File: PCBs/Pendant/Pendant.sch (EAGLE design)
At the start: 17 parts

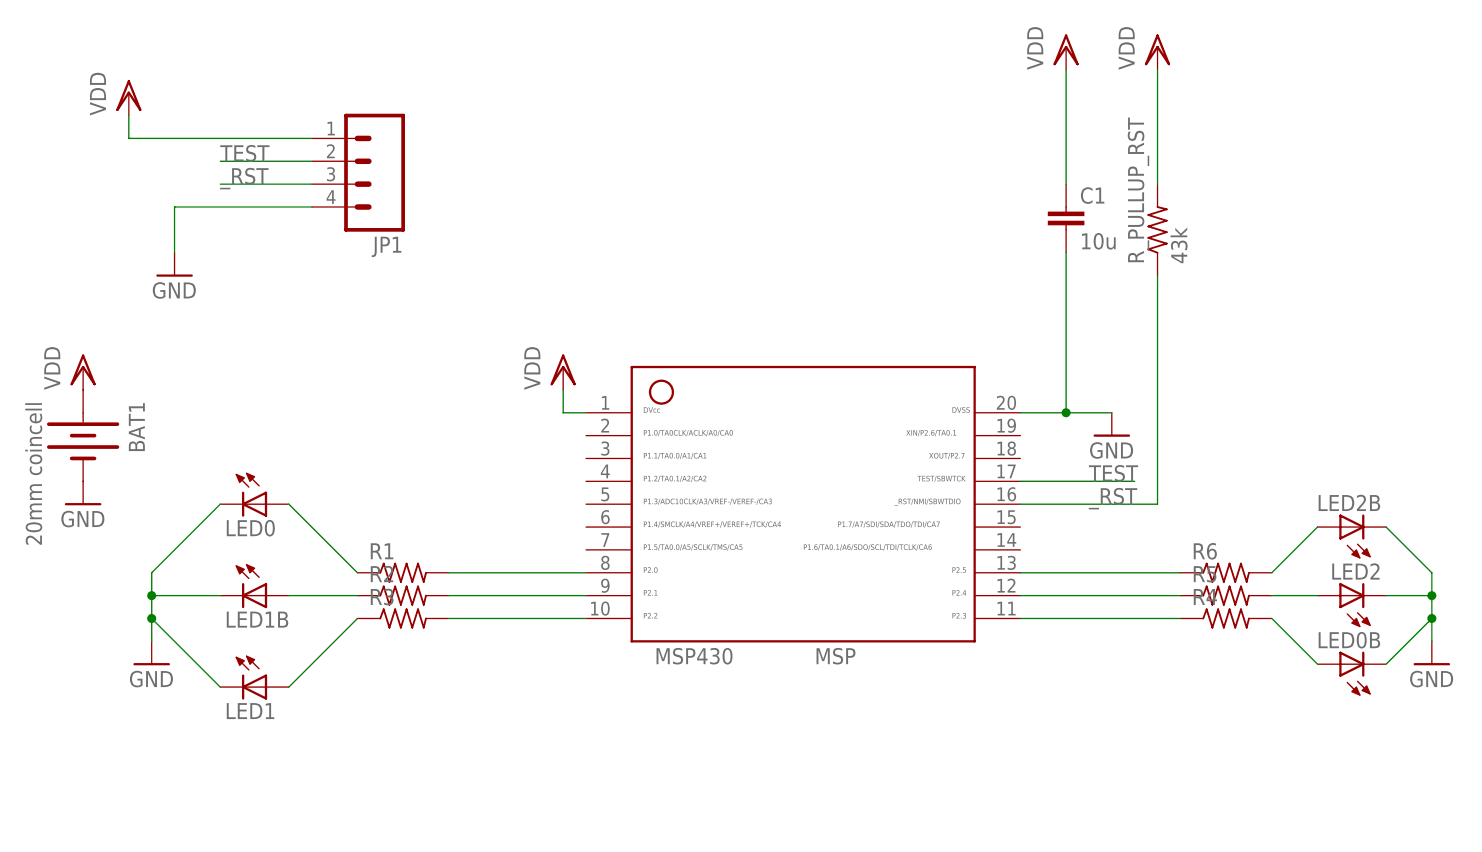
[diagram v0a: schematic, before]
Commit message: Updated pendant to 2017 version
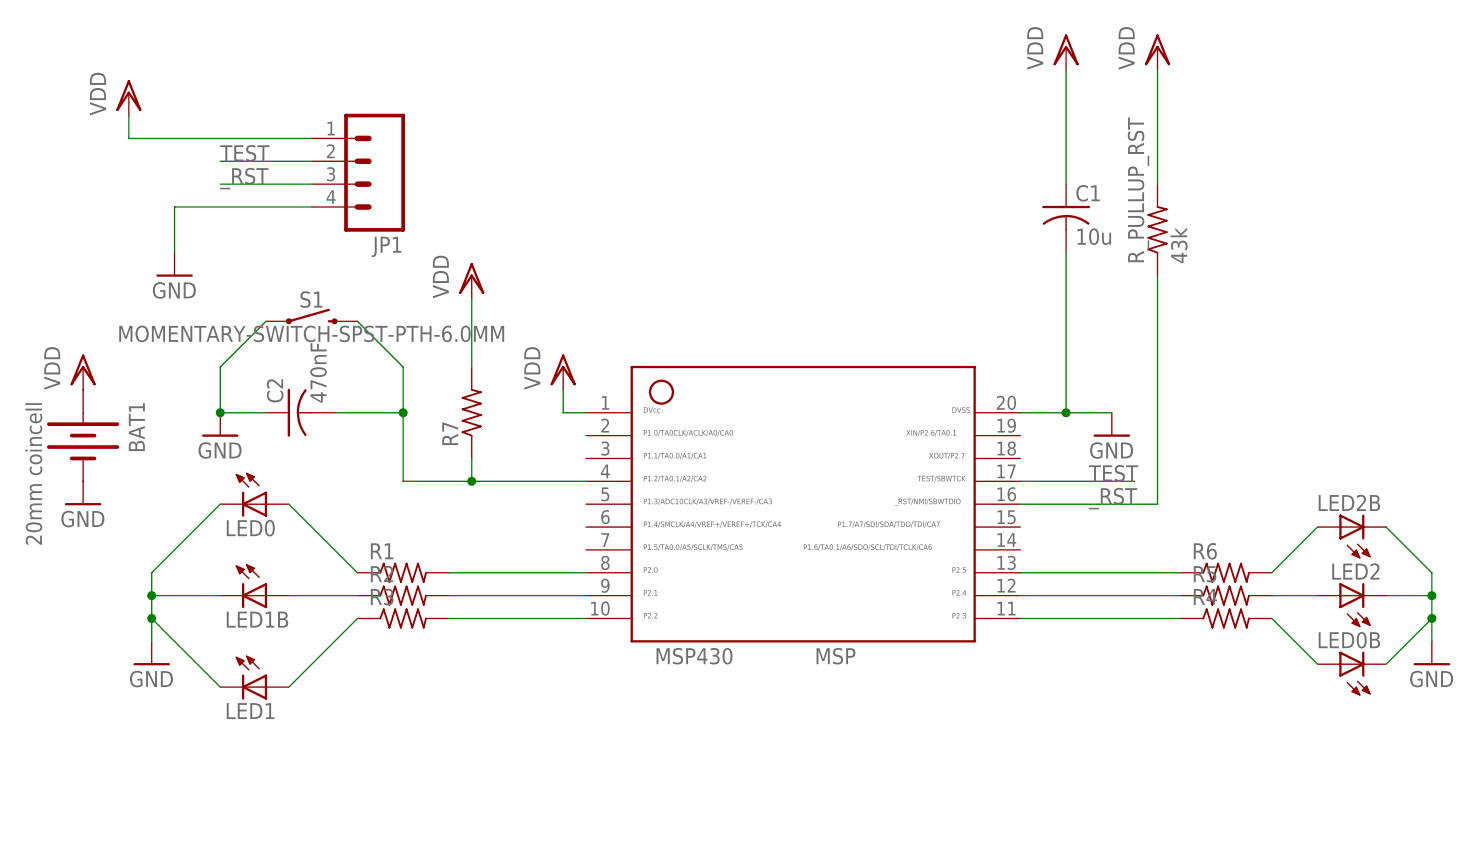
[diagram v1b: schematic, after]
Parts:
- added C2: 470nF, rcl:C-USC1206
- added R7: (no value), rcl:R-US_R1206
- added S1: MOMENTARY-SWITCH-SPST-PTH-6.0MM, SparkFun-Switches:MOMENTARY-SWITCH-SPST-PTH-6.0MM
- C1: device rcl:C-EUC0603 -> rcl:C-USC1206
- R1, R2, R3, R4, R5, R6, R_PULLUP_RST: device BiphasicBoard:R-US_R0603 -> rcl:R-US_R1206
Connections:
- new net N$14: C2.2, MSP430.4, R7.1, S1.2
- net GND: now also C2.1, S1.1
- net VDD: now also R7.2
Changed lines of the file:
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@@
 <?xml version="1.0" encoding="utf-8"?>
 <!DOCTYPE eagle SYSTEM "eagle.dtd">
-<eagle version="7.5.0">
+<eagle version="7.7.0">
 <drawing>
 <settings>
@@
 <layer number="113" name="IDFDebug" color="4" fill="1" visible="no" active="yes"/>
 <layer number="116" name="Patch_BOT" color="9" fill="4" visible="yes" active="yes"/>
+<layer number="118" name="Rect_Pads" color="7" fill="1" visible="no" active="yes"/>
 <layer number="121" name="tTestdril" color="7" fill="1" visible="yes" active="yes"/>
 <layer number="122" name="bTestdril" color="7" fill="1" visible="yes" active="yes"/>
@@
 <layer number="251" name="SMDround" color="12" fill="11" visible="no" active="no"/>
 <layer number="254" name="OrgLBR" color="7" fill="1" visible="yes" active="yes"/>
+<layer number="255" name="routoute" color="7" fill="1" visible="no" active="yes"/>
 </layers>
 <schematic xreflabel="%F%N/%S.%C%R" xrefpart="/%S.%C%R">
@@
 </classes>
 <parts>
-<part name="R_PULLUP_RST" library="BiphasicBoard" deviceset="R-US_" device="R0603" value="43k"/>
+<part name="R_PULLUP_RST" library="rcl" deviceset="R-US_" device="R1206" value="43k"/>
 <part name="MSP430" library="RatDBS" deviceset="MSP430" device="" value="MSP"/>
 <part name="LED2B" library="SparkFun-LED" deviceset="LED" device="1206"/>
-<part name="R6" library="BiphasicBoard" deviceset="R-US_" device="R0603"/>
+<part name="R6" library="rcl" deviceset="R-US_" device="R1206"/>
 <part name="JP1" library="Pendant" deviceset="M04" device="LOCK"/>
 <part name="VDD1" library="supply1" deviceset="VDD" device=""/>
@@
 <part name="VDD11" library="supply1" deviceset="VDD" device=""/>
 <part name="GND11" library="supply1" deviceset="GND" device=""/>
-<part name="C1" library="rcl" deviceset="C-EU" device="C0603" value="10u"/>
-<part name="R1" library="BiphasicBoard" deviceset="R-US_" device="R0603"/>
-<part name="R2" library="BiphasicBoard" deviceset="R-US_" device="R0603"/>
-<part name="R3" library="BiphasicBoard" deviceset="R-US_" device="R0603"/>
-<part name="R5" library="BiphasicBoard" deviceset="R-US_" device="R0603"/>
-<part name="R4" library="BiphasicBoard" deviceset="R-US_" device="R0603"/>
+<part name="C1" library="rcl" deviceset="C-US" device="C1206" value="10u"/>
+<part name="R1" library="rcl" deviceset="R-US_" device="R1206"/>
+<part name="R2" library="rcl" deviceset="R-US_" device="R1206"/>
+<part name="R3" library="rcl" deviceset="R-US_" device="R1206"/>
+<part name="R5" library="rcl" deviceset="R-US_" device="R1206"/>
+<part name="R4" library="rcl" deviceset="R-US_" device="R1206"/>
 <part name="LED2" library="SparkFun-LED" deviceset="LED" device="1206"/>
 <part name="LED0B" library="SparkFun-LED" deviceset="LED" device="1206"/>
@@
 <part name="GND1" library="supply1" deviceset="GND" device=""/>
 <part name="GND2" library="supply1" deviceset="GND" device=""/>
+<part name="S1" library="SparkFun-Switches" deviceset="MOMENTARY-SWITCH-SPST" device="-PTH-6.0MM"/>
+<part name="VDD2" library="supply1" deviceset="VDD" device=""/>
+<part name="R7" library="rcl" deviceset="R-US_" device="R1206"/>
+<part name="GND3" library="supply1" deviceset="GND" device=""/>
+<part name="C2" library="rcl" deviceset="C-US" device="C1206" value="470nF"/>
 </parts>
 <sheets>
@@
 <instance part="GND1" gate="1" x="-71.12" y="-17.78"/>
 <instance part="GND2" gate="1" x="71.12" y="-17.78"/>
+<instance part="S1" gate="G$1" x="-53.34" y="20.32"/>
+<instance part="VDD2" gate="G$1" x="-35.56" y="25.4"/>
+<instance part="R7" gate="G$1" x="-35.56" y="10.16" rot="R90"/>
+<instance part="GND3" gate="1" x="-63.5" y="7.62"/>
+<instance part="C2" gate="G$1" x="-55.88" y="10.16" rot="R90"/>
 </instances>
 <busses>
@@
 <pinref part="BAT1" gate="G$1" pin="+"/>
 <pinref part="VDD11" gate="G$1" pin="VDD"/>
+</segment>
+<segment>
+<pinref part="VDD2" gate="G$1" pin="VDD"/>
+<pinref part="R7" gate="G$1" pin="2"/>
+<wire x1="-35.56" y1="22.86" x2="-35.56" y2="15.24" width="0.1524" layer="91"/>
 </segment>
 </net>
@@
 <pinref part="GND6" gate="1" pin="GND"/>
 </segment>
+<segment>
+<pinref part="S1" gate="G$1" pin="1"/>
+<wire x1="-58.42" y1="20.32" x2="-63.5" y2="15.24" width="0.1524" layer="91"/>
+<wire x1="-63.5" y1="15.24" x2="-63.5" y2="10.16" width="0.1524" layer="91"/>
+<pinref part="GND3" gate="1" pin="GND"/>
+<pinref part="C2" gate="G$1" pin="1"/>
+<wire x1="-58.42" y1="10.16" x2="-63.5" y2="10.16" width="0.1524" layer="91"/>
+<junction x="-63.5" y="10.16"/>
+</segment>
 </net>
 <net name="TEST" class="0">
@@
 </segment>
 </net>
+<net name="N$14" class="0">
+<segment>
+<pinref part="R7" gate="G$1" pin="1"/>
+<wire x1="-35.56" y1="5.08" x2="-35.56" y2="2.54" width="0.1524" layer="91"/>
+<pinref part="MSP430" gate="G$1" pin="4"/>
+<wire x1="-35.56" y1="2.54" x2="-22.86" y2="2.54" width="0.1524" layer="91"/>
+<pinref part="S1" gate="G$1" pin="2"/>
+<wire x1="-48.26" y1="20.32" x2="-43.18" y2="15.24" width="0.1524" layer="91"/>
+<wire x1="-43.18" y1="15.24" x2="-43.18" y2="10.16" width="0.1524" layer="91"/>
+<wire x1="-43.18" y1="10.16" x2="-43.18" y2="2.54" width="0.1524" layer="91"/>
+<wire x1="-43.18" y1="2.54" x2="-35.56" y2="2.54" width="0.1524" layer="91"/>
+<junction x="-35.56" y="2.54"/>
+<pinref part="C2" gate="G$1" pin="2"/>
+<wire x1="-50.8" y1="10.16" x2="-43.18" y2="10.16" width="0.1524" layer="91"/>
+<junction x="-43.18" y="10.16"/>
+</segment>
+</net>

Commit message: Updated Pendant Eagle files
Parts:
- removed LED0, LED0B, LED1B, LED2B: (no value), SparkFun-LED:LED1206
- added LED3, LED4, LED5, LED6, LED7, LED8: (no value), led:LEDCHIPLED_1206
- added R8, R9: (no value), rcl:R-US_R1206
- LED1, LED2: device SparkFun-LED:LED1206 -> led:LEDCHIPLED_1206
- R10: value 43k -> (none)
- renumbered R_PULLUP_RST to R10
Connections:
- net N$1 renamed D5
- net N$2 renamed D4
- net N$5 renamed D6
- removed net N$10: LED1.A, R3.1
- removed net N$11: MSP430.8, R1.2
- removed net N$12: MSP430.9, R2.2
- removed net N$13: MSP430.10, R3.2
- removed net N$9: LED2B.A, R6.2
- new net D1: MSP430.8, R1.1
- new net D2: MSP430.9, R2.1
- new net D3: MSP430.10, R3.1
- new net D7: MSP430.14, R7.1
- new net D8: MSP430.15, R8.1
- new net N$1: LED1.A, R1.2
- new net N$2: LED2.A, R2.2
- new net N$5: LED5.A, R5.2
- net GND: now also LED3.C, LED4.C, LED5.C, LED6.C, LED7.C, LED8.C; no longer LED0.C, LED0B.C, LED1B.C, LED2B.C
- net N$14: now also R9.2; no longer R7.1
- net N$3: now also LED3.A, R3.2; no longer LED2.A, R5.2
- net N$4: now also LED4.A; no longer LED0B.A
- net N$6: now also LED6.A, R6.2; no longer MSP430.7
- net N$7: now also LED7.A, R7.2; no longer LED0.A, R1.1
- net N$8: now also LED8.A, R8.2; no longer LED1B.A, R2.1
- net VDD: now also R10.1, R9.1; no longer R10.2, R7.2
- net _RST: now also R10.2; no longer R10.1
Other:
- moved on the sheet: LED1, LED2, R1, R2, R3, R4, R5, R6, R7
